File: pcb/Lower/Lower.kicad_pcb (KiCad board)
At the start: 2 copper layers, 52 x 40 mm, 35 parts, among them J1 AudioJack3, J2 AudioJack3, J3 Barrel_Jack, J4 Conn_01x04, Q1 AO3401A, SW1 SW_Push_3PDT, U1 TL072

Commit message: [Lower] Push some parts around a bit
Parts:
- moved C1 0.25 mm to (136.4, 118.4)

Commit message: [Lower] Fix DRC violations
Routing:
- net /Input: track 23.5 -> 22.3 mm
- net /Output: track 43.2 -> 42.3 mm
- net Net-(D1-Pad1): track 20.8 -> 20.0 mm
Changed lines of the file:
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@@
   (segment (start 136.787 116.641) (end 136.352888 117.075112) (width 0.4) (layer "F.Cu") (net 1))
   (segment (start 124.354 109.77) (end 128.672 114.088) (width 0.4) (layer "F.Cu") (net 1))
-  (segment (start 136.787 118.225888) (end 136.606888 118.406) (width 0.4) (layer "F.Cu") (net 1))
   (segment (start 141.372 102.404) (end 142.388 101.388) (width 0.4) (layer "F.Cu") (net 1))
   (segment (start 136.787 116.12) (end 136.787 116.641) (width 0.4) (layer "F.Cu") (net 1))
@@
   (via (at 154.072 101.134) (size 1) (drill 0.6) (layers "F.Cu" "B.Cu") (net 8))
   (segment (start 152.166 101.134) (end 154.072 101.134) (width 0.4) (layer "B.Cu") (net 8))
-  (segment (start 149.5 104.69) (end 149.5 103.8) (width 0.4) (layer "B.Cu") (net 8))
   (segment (start 149.5 103.8) (end 152.166 101.134) (width 0.4) (layer "B.Cu") (net 8))
   (segment (start 166.518 102.658) (end 166.518 101.705) (width 0.4) (layer "F.Cu") (net 9))
@@
   (segment (start 165.756 108.5) (end 165.756 103.42) (width 0.4) (layer "F.Cu") (net 9))
   (segment (start 159.152 85.64) (end 158.14 85.64) (width 0.4) (layer "F.Cu") (net 10))
-  (segment (start 154.8 108.5) (end 154.8 108.212) (width 0.4) (layer "F.Cu") (net 10))
   (segment (start 152.294 105.994) (end 154.8 108.5) (width 0.4) (layer "F.Cu") (net 10))
   (segment (start 158.14 85.64) (end 157 84.5) (width 0.4) (layer "F.Cu") (net 10))
@@
   (segment (start 137.562 92.498) (end 138.832 91.228) (width 0.4) (layer "F.Cu") (net 12))
   (segment (start 139.086 91.228) (end 143.667 91.228) (width 0.4) (layer "F.Cu") (net 12))
-  (segment (start 143.895 91) (end 143.695479 91.199521) (width 0.4) (layer "B.Cu") (net 12))
-  (segment (start 143.895 91) (end 143 91) (width 0.4) (layer "B.Cu") (net 12))
   (segment (start 137.562 105.743) (end 137.562 96.017) (width 0.4) (layer "F.Cu") (net 13))
   (segment (start 160.602 85.64) (end 162.899 85.64) (width 0.4) (layer "F.Cu") (net 14))
@@
   (segment (start 146.706 105.994) (end 144.2 108.5) (width 0.4) (layer "B.Cu") (net 18))
   (segment (start 147.976 101.896) (end 146.706 103.166) (width 0.4) (layer "B.Cu") (net 18))
-  (segment (start 155.1 96) (end 156 96) (width 0.4) (layer "B.Cu") (net 18))
   (segment (start 147.976 95.038) (end 147.976 101.896) (width 0.4) (layer "B.Cu") (net 18))
   (segment (start 147.468 102.404) (end 153.872 96) (width 0.4) (layer "B.Cu") (net 18))
@@
   (segment (start 135.276 110.532) (end 137.562 108.246) (width 0.4) (layer "F.Cu") (net 22))
   (segment (start 148.23 106.214) (end 152.386 106.214) (width 0.4) (layer "B.Cu") (net 22))
-  (segment (start 144.2 113.2) (end 144.292 113.2) (width 0.4) (layer "B.Cu") (net 22))
+  (segment (start 146.706 110.694) (end 144.2 113.2) (width 0.4) (layer "B.Cu") (net 22))
   (segment (start 152.386 106.214) (end 154.8 103.8) (width 0.4) (layer "B.Cu") (net 22))
   (segment (start 146.706 110.694) (end 146.706 107.738) (width 0.4) (layer "B.Cu") (net 22))
   (segment (start 146.706 107.738) (end 148.23 106.214) (width 0.4) (layer "B.Cu") (net 22))
-  (segment (start 144.2 113.2) (end 146.706 110.694) (width 0.4) (layer "B.Cu") (net 22))
   (zone (net 2) (net_name "GND") (layers F&B.Cu) (name "GNDpour") (hatch edge 0.508)
     (connect_pads (clearance 0.508))

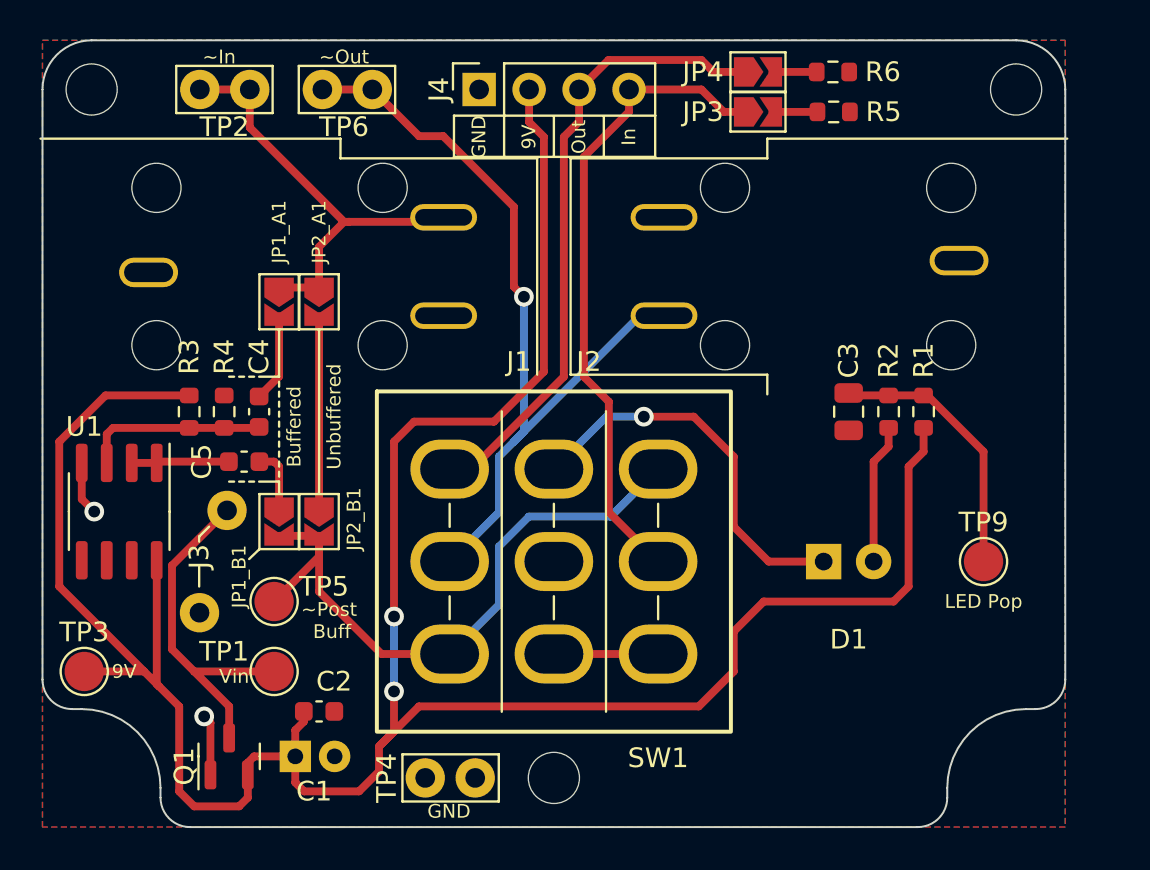
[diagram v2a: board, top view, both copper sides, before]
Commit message: [Lower] Beautify silk and add logos
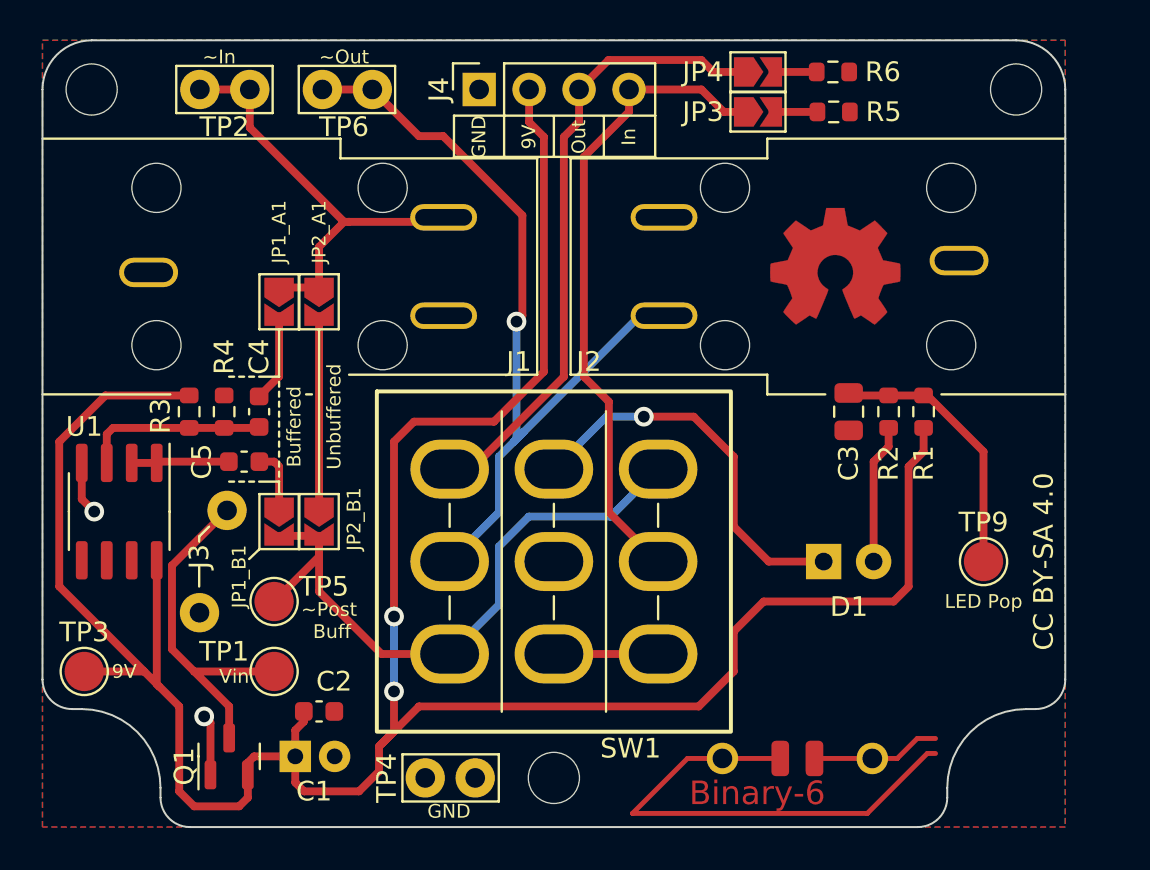
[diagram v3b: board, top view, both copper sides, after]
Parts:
- added H7: Symbol_Binary6, MeineBib:Binary_6_v0.1_tiny_silk, F.Cu at (161.9, 119.5)
- added MK6: PentThin, MeineBib:PentThin, B.Cu at (163.8, 93.6)
- added REF**: OSHW-Symbol_6.7x6mm_Copper, Symbol:OSHW-Symbol_6.7x6mm_Copper, F.Cu at (163.8, 93.5)
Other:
- board text added: "CC BY-SA 4.0"
- board text added: "Chrismettal 2022_02"
- board text added: "JLCJLCJLCJLC"

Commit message: [Lower] Beautify silk - should be ready to order
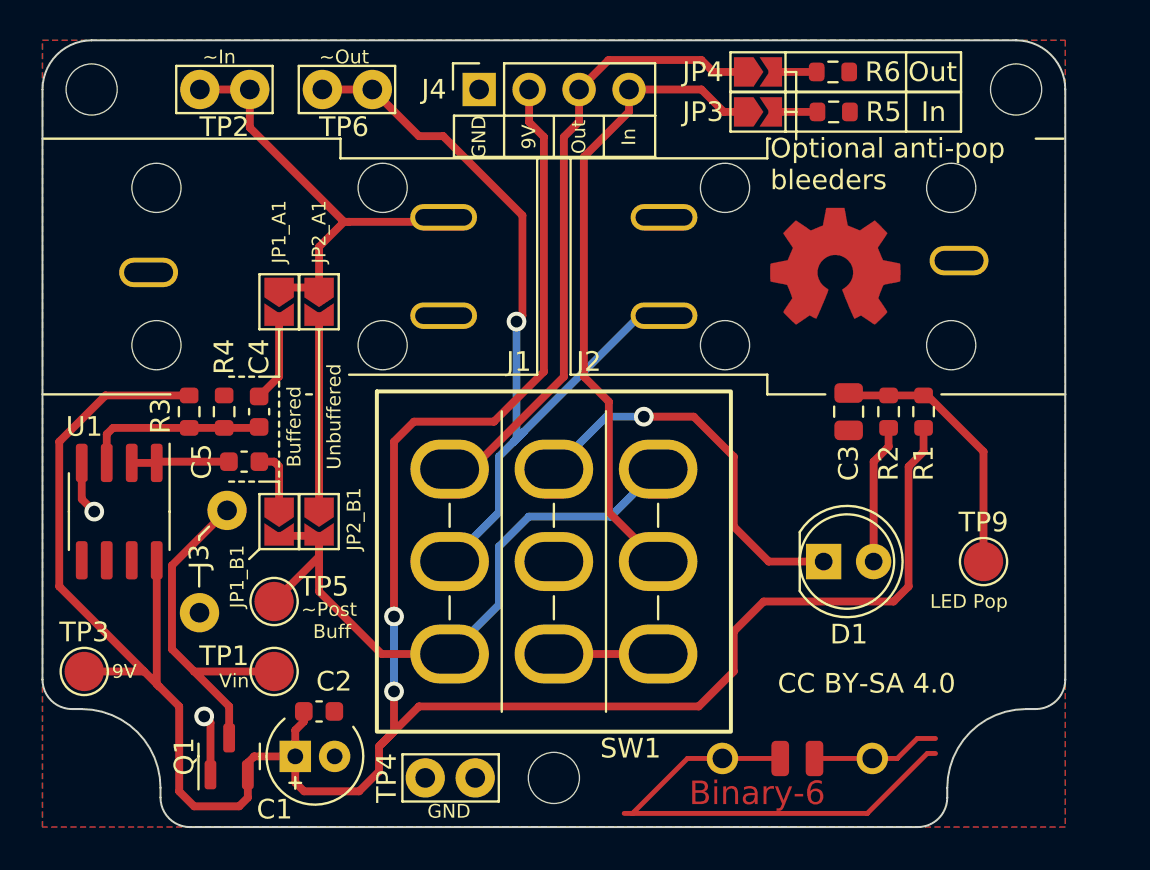
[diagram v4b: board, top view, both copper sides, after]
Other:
- board text added: "If you can read this the PCB is installed wrong"
- board text added: "Optional anti-pop bleeders"
- board text added: "This side towards foot"

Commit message: [Lower] Update commit hash
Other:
- board text added: "${Commit}"
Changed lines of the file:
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@@
     )
   )
-  (property "Commit" "abcd123")
+  (property "Commit" "e9c2911")
   (net 0 "")
   (net 1 "+9V")
@@
     (effects (font (size 0.7 0.7) (thickness 0.13)))
   )
+  (gr_text "${Commit}" (at 125.4 93.5 270) (layer "F.SilkS")
+    (effects (font (size 1 1) (thickness 0.2)))
+  )
   (gr_text "9V" (at 148.23 86.91 90) (layer "F.SilkS")
